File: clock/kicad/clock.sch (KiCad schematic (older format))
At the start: 79 parts, among them SW1 HOUR, SW2 MIN, SW3 TIME, U1 74HC4060, U10 74HC4511, U11 74HC4511, U12 74HC4511, U13 74HC4511, U14 KCSC02-105, U15 KCSC02-105, U16 KCSC02-105, U17 KCSC02-105, U18 KCSC02-105, U19 KCSC02-105, U2 SN74HC74N, U20 74HC14, U21 74HC157, U3 74HC390, U4 74HC08, U5 74HC390, U6 74HC08, U7 74HC390, U8 74HC4511, U9 74HC4511

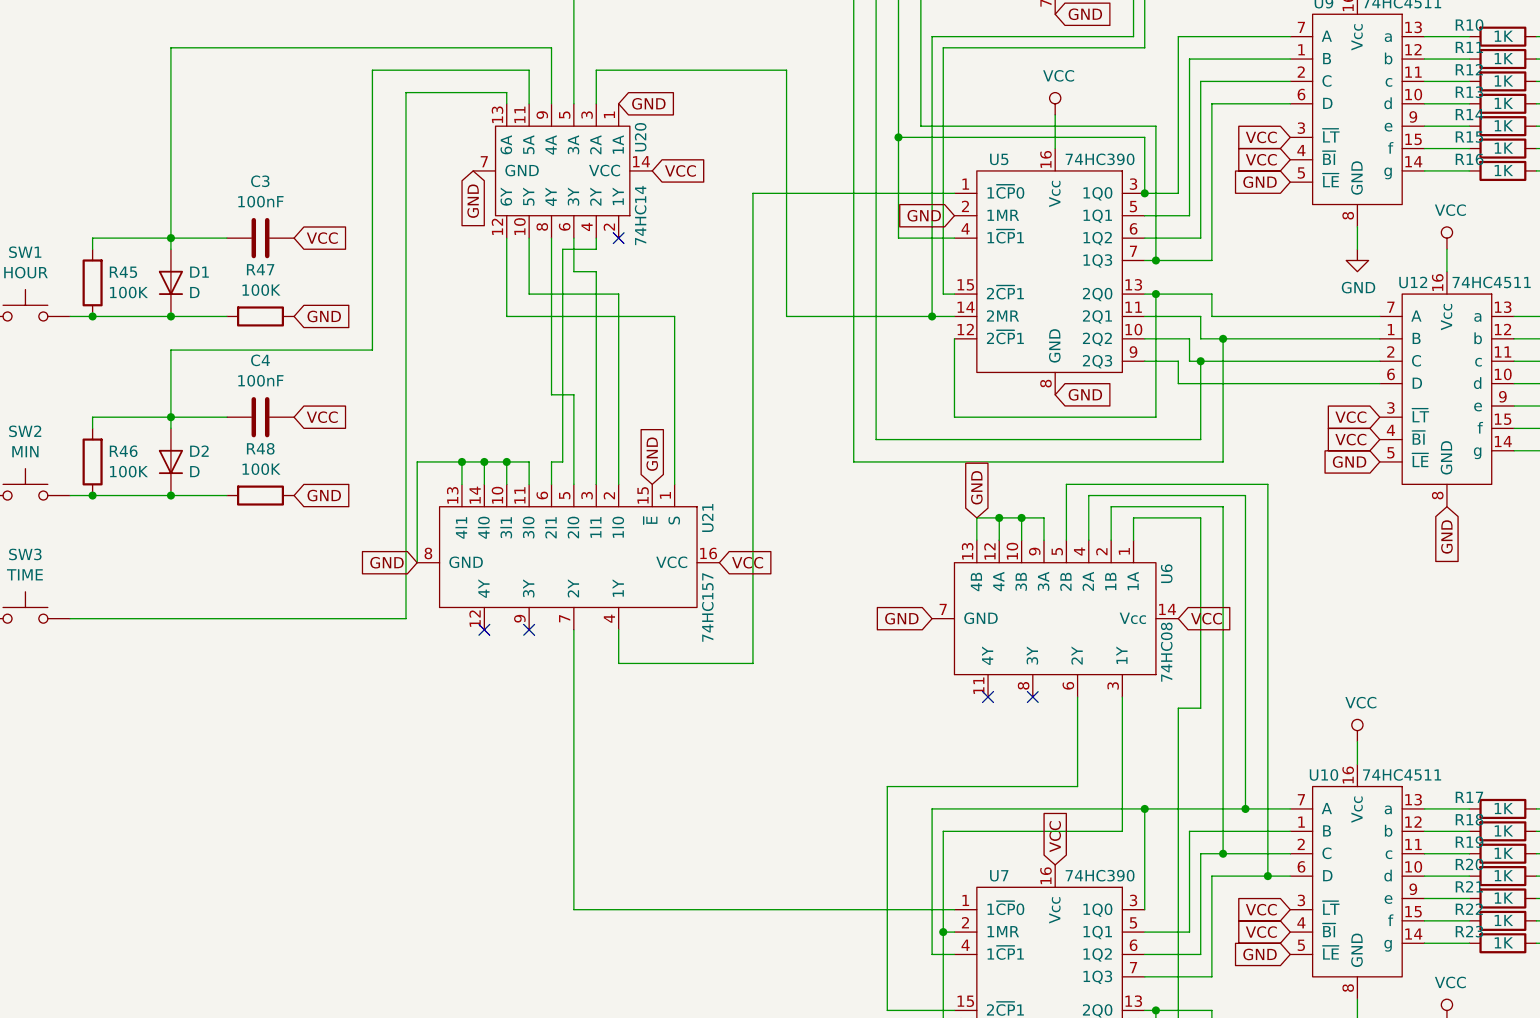
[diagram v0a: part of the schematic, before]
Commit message: Clock: Created PCB Layout.
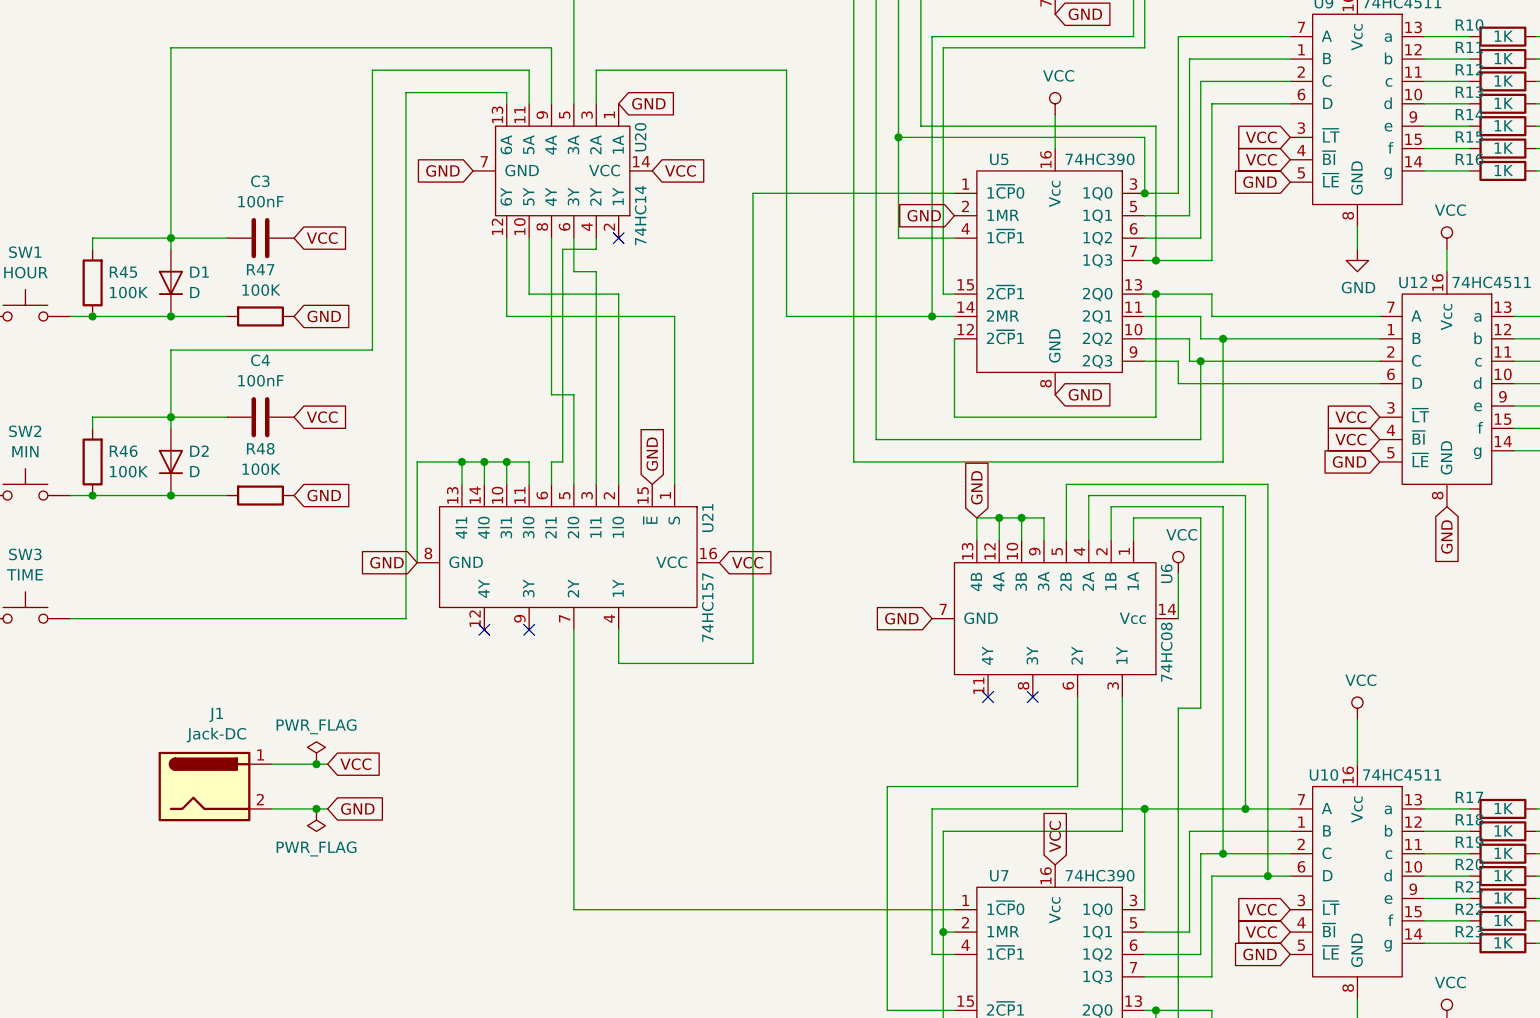
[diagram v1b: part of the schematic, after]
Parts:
- added J1: Jack-DC, KiCad:BarrelJack_CUI_PJ-063AH_Horizontal, symbol Connector:Jack-DC
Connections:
- net GND: now also J1.2
- net VCC: now also J1.1
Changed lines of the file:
@@
 L power:VCC #PWR014
 U 1 1 5D45B0C8
-P 7100 7950
-F 0 "#PWR014" H 7100 7800 50  0001 C CNN
-F 1 "VCC" H 7117 8123 50  0000 C CNN
-F 2 "" H 7100 7950 50  0001 C CNN
-F 3 "" H 7100 7950 50  0001 C CNN
-	1    7100 7950
+P 7100 7850
+F 0 "#PWR014" H 7100 7700 50  0001 C CNN
+F 1 "VCC" H 7117 8023 50  0000 C CNN
+F 2 "" H 7100 7850 50  0001 C CNN
+F 3 "" H 7100 7850 50  0001 C CNN
+	1    7100 7850
 	1    0    0    -1
 $EndComp
@@
 	7100 9100 7100 9200
 Wire Wire Line
-	7100 7950 7100 8050
-Wire Wire Line
 	7500 9200 7500 9300
 Text GLabel 6800 8800 0    50   Input ~ 0
@@
 	5200 8900 5300 8900
 Connection ~ 5200 6050
-Text GLabel 6300 7400 2    50   Input ~ 0
-VCC
 Text GLabel 5200 7400 0    50   Input ~ 0
 GND
@@
 Wire Wire Line
 	1350 7400 2850 7400
-Text GLabel 3150 5400 3    50   Input ~ 0
+Text GLabel 3150 5400 0    50   Input ~ 0
 GND
 Text GLabel 3950 5400 2    50   Input ~ 0
@@
 Connection ~ 3100 6700
 NoConn ~ 3800 5700
+Text GLabel 2900 7150 0    50   Input ~ 0
+GND
+Text GLabel 4250 7150 2    50   Input ~ 0
+VCC
+Wire Wire Line
+	2850 7400 2850 5050
+Wire Wire Line
+	2850 5050 3300 5050
+Wire Wire Line
+	3300 5050 3300 5100
+Wire Wire Line
+	3400 4950 2700 4950
+Wire Wire Line
+	2700 4950 2700 6200
+Wire Wire Line
+	3400 4950 3400 5100
+Wire Wire Line
+	1800 4850 3500 4850
+Wire Wire Line
+	3500 4850 3500 5100
+Wire Wire Line
+	1800 4850 1800 5700
+Wire Wire Line
+	3300 5700 3300 6050
+Wire Wire Line
+	3400 5700 3400 5950
+Wire Wire Line
+	5100 3300 3600 3300
+Wire Wire Line
+	3600 3300 3600 5100
+Connection ~ 5100 3300
+Text GLabel 3800 5100 2    50   Input ~ 0
+GND
+Wire Wire Line
+	5300 5500 4400 5500
+Wire Wire Line
+	4400 5500 4400 7600
+Wire Wire Line
+	4550 6050 4550 4950
+Wire Wire Line
+	4550 4950 3700 4950
+Wire Wire Line
+	3700 4950 3700 5100
+Wire Wire Line
+	4550 6050 5200 6050
+Wire Wire Line
+	4050 6050 4050 6800
+Wire Wire Line
+	3300 6050 4050 6050
+Wire Wire Line
+	3600 7450 3600 8700
+Wire Wire Line
+	3600 8700 5300 8700
+Wire Wire Line
+	3800 7450 3800 7600
+Wire Wire Line
+	3800 7600 4400 7600
+Wire Wire Line
+	3500 5700 3500 6400
+Wire Wire Line
+	3600 6800 3600 6400
+Wire Wire Line
+	3600 6400 3500 6400
+Wire Wire Line
+	3400 5950 3800 5950
+Wire Wire Line
+	3800 5950 3800 6800
+Text GLabel 3950 6800 1    50   Input ~ 0
+GND
+Wire Wire Line
+	3700 5700 3700 5750
+Wire Wire Line
+	3700 5750 3550 5750
+Wire Wire Line
+	3550 6700 3500 6700
+Wire Wire Line
+	3500 6700 3500 6800
+Wire Wire Line
+	2900 7150 2900 6700
+Wire Wire Line
+	2900 6700 3100 6700
+$Comp
+L power:VCC #PWR0101
+U 1 1 5D33EDBB
+P 6300 7200
+F 0 "#PWR0101" H 6300 7050 50  0001 C CNN
+F 1 "VCC" H 6317 7373 50  0000 C CNN
+F 2 "" H 6300 7200 50  0001 C CNN
+F 3 "" H 6300 7200 50  0001 C CNN
+	1    6300 7200
+	1    0    0    -1
+$EndComp
+Wire Wire Line
+	6300 7200 6300 7400
+Wire Wire Line
+	7100 7850 7100 8050
+Wire Wire Line
+	3700 6800 3700 5850
+Wire Wire Line
+	3700 5850 3600 5850
+Wire Wire Line
+	3600 5850 3600 5700
+$Comp
+L Connector:Jack-DC J1
+U 1 1 5D0C7F55
+P 1950 8150
+F 0 "J1" H 2007 8475 50  0000 C CNN
+F 1 "Jack-DC" H 2007 8384 50  0000 C CNN
+F 2 "KiCad:BarrelJack_CUI_PJ-063AH_Horizontal" H 2000 8110 50  0001 C CNN
+F 3 "~" H 2000 8110 50  0001 C CNN
+	1    1950 8150
+	1    0    0    -1
+$EndComp
+Text GLabel 2500 8050 2    50   Input ~ 0
+VCC
+Text GLabel 2500 8250 2    50   Input ~ 0
+GND
+Wire Wire Line
+	2500 8050 2450 8050
+Wire Wire Line
+	2250 8250 2450 8250
+$Comp
+L power:PWR_FLAG #FLG0101
+U 1 1 5D14D41D
+P 2450 8050
+F 0 "#FLG0101" H 2450 8125 50  0001 C CNN
+F 1 "PWR_FLAG" H 2450 8223 50  0000 C CNN
+F 2 "" H 2450 8050 50  0001 C CNN
+F 3 "~" H 2450 8050 50  0001 C CNN
+	1    2450 8050
+	1    0    0    -1
+$EndComp
+Connection ~ 2450 8050
+Wire Wire Line
+	2450 8050 2250 8050
+$Comp
+L power:PWR_FLAG #FLG0102
+U 1 1 5D2210FE
+P 2450 8250
+F 0 "#FLG0102" H 2450 8325 50  0001 C CNN
+F 1 "PWR_FLAG" H 2450 8423 50  0000 C CNN
+F 2 "" H 2450 8250 50  0001 C CNN
+F 3 "~" H 2450 8250 50  0001 C CNN
+	1    2450 8250
+	-1   0    0    1
+$EndComp
+Connection ~ 2450 8250
+Wire Wire Line
+	2450 8250 2500 8250
+Wire Wire Line
+	3550 5750 3550 6700
 $Comp
 L clock:74HC14 U20
@@
 	0    1    1    0
 $EndComp
-Text GLabel 2900 7150 0    50   Input ~ 0
-GND
-Text GLabel 4250 7150 2    50   Input ~ 0
-VCC
-Wire Wire Line
-	2850 7400 2850 5050
-Wire Wire Line
-	2850 5050 3300 5050
-Wire Wire Line
-	3300 5050 3300 5100
-Wire Wire Line
-	3400 4950 2700 4950
-Wire Wire Line
-	2700 4950 2700 6200
-Wire Wire Line
-	3400 4950 3400 5100
-Wire Wire Line
-	1800 4850 3500 4850
-Wire Wire Line
-	3500 4850 3500 5100
-Wire Wire Line
-	1800 4850 1800 5700
-Wire Wire Line
-	3300 5700 3300 6050
-Wire Wire Line
-	3400 5700 3400 5950
-Wire Wire Line
-	5100 3300 3600 3300
-Wire Wire Line
-	3600 3300 3600 5100
-Connection ~ 5100 3300
-Wire Wire Line
-	3600 5700 3600 5850
-Text GLabel 3800 5100 2    50   Input ~ 0
-GND
-Wire Wire Line
-	5300 5500 4400 5500
-Wire Wire Line
-	4400 5500 4400 7600
-Wire Wire Line
-	4550 6050 4550 4950
-Wire Wire Line
-	4550 4950 3700 4950
-Wire Wire Line
-	3700 4950 3700 5100
-Wire Wire Line
-	4550 6050 5200 6050
-Wire Wire Line
-	4050 6050 4050 6800
-Wire Wire Line
-	3300 6050 4050 6050
-Wire Wire Line
-	3600 7450 3600 8700
-Wire Wire Line
-	3600 8700 5300 8700
-Wire Wire Line
-	3800 7450 3800 7600
-Wire Wire Line
-	3800 7600 4400 7600
-Wire Wire Line
-	3500 5700 3500 6400
-Wire Wire Line
-	3600 6800 3600 6400
-Wire Wire Line
-	3600 6400 3500 6400
-Wire Wire Line
-	3600 5850 3700 5850
-Wire Wire Line
-	3700 5850 3700 6800
-Wire Wire Line
-	3400 5950 3800 5950
-Wire Wire Line
-	3800 5950 3800 6800
-Text GLabel 3950 6800 1    50   Input ~ 0
-GND
-Wire Wire Line
-	3700 5700 3700 5750
-Wire Wire Line
-	3700 5750 3550 5750
-Wire Wire Line
-	3550 5750 3550 6700
-Wire Wire Line
-	3550 6700 3500 6700
-Wire Wire Line
-	3500 6700 3500 6800
-Wire Wire Line
-	2900 7150 2900 6700
-Wire Wire Line
-	2900 6700 3100 6700
 $EndSCHEMATC

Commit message: Clock: Added Decoupling Capacitors.
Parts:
- added C10, C11, C12, C13, C14, C15, C16, C17, C18, C19, C5, C6, C8, C9: 100nF, Capacitor_THT:C_Disc_D5.0mm_W2.5mm_P2.50mm, symbol Device:C
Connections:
- net GND: now also C10.2, C11.2, C12.2, C13.2, C14.2, C15.2, C16.2, C17.2, C18.2, C19.2, C5.2, C6.2, C8.2, C9.1
- net VCC: now also C10.1, C11.1, C12.1, C13.1, C14.1, C15.1, C16.1, C17.1, C18.1, C19.1, C5.1, C6.1, C8.1, C9.2

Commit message: Clock: Added USB power connector.
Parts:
- removed J1: Jack-DC, KiCad:BarrelJack_CUI_PJ-063AH_Horizontal, symbol Connector:Jack-DC
- added J1: USB-SS-52100-001, KiCad:USB_A_Stewart_SS-52100-001_Horizontal, symbol clock:USB-SS-52100-001
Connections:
- net GND: now also J1.4 (GND), J1.5 (SHELL)
- net VCC: now also J1.1 (VCC)
- no-connect marks 30 -> 32
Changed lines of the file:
@@
 Wire Wire Line
 	3600 5850 3600 5700
-$Comp
-L Connector:Jack-DC J1
-U 1 1 5D0C7F55
-P 1950 8150
-F 0 "J1" H 2007 8475 50  0000 C CNN
-F 1 "Jack-DC" H 2007 8384 50  0000 C CNN
-F 2 "KiCad:BarrelJack_CUI_PJ-063AH_Horizontal" H 2000 8110 50  0001 C CNN
-F 3 "~" H 2000 8110 50  0001 C CNN
-	1    1950 8150
-	1    0    0    -1
-$EndComp
-Text GLabel 2500 8050 2    50   Input ~ 0
+Text GLabel 2150 8300 2    50   Input ~ 0
 VCC
-Text GLabel 2500 8250 2    50   Input ~ 0
-GND
-Wire Wire Line
-	2500 8050 2450 8050
-Wire Wire Line
-	2250 8250 2450 8250
+Text GLabel 2150 8000 2    50   Input ~ 0
+GND
+Wire Wire Line
+	2150 8300 2100 8300
 $Comp
 L power:PWR_FLAG #FLG0101
 U 1 1 5D14D41D
-P 2450 8050
-F 0 "#FLG0101" H 2450 8125 50  0001 C CNN
-F 1 "PWR_FLAG" H 2450 8223 50  0000 C CNN
-F 2 "" H 2450 8050 50  0001 C CNN
-F 3 "~" H 2450 8050 50  0001 C CNN
-	1    2450 8050
-	1    0    0    -1
-$EndComp
-Connection ~ 2450 8050
-Wire Wire Line
-	2450 8050 2250 8050
+P 2100 8300
+F 0 "#FLG0101" H 2100 8375 50  0001 C CNN
+F 1 "PWR_FLAG" H 2100 8473 50  0000 C CNN
+F 2 "" H 2100 8300 50  0001 C CNN
+F 3 "~" H 2100 8300 50  0001 C CNN
+	1    2100 8300
+	1    0    0    -1
+$EndComp
+Connection ~ 2100 8300
 $Comp
 L power:PWR_FLAG #FLG0102
 U 1 1 5D2210FE
-P 2450 8250
-F 0 "#FLG0102" H 2450 8325 50  0001 C CNN
-F 1 "PWR_FLAG" H 2450 8423 50  0000 C CNN
-F 2 "" H 2450 8250 50  0001 C CNN
-F 3 "~" H 2450 8250 50  0001 C CNN
-	1    2450 8250
-	-1   0    0    1
-$EndComp
-Connection ~ 2450 8250
-Wire Wire Line
-	2450 8250 2500 8250
+P 2100 8000
+F 0 "#FLG0102" H 2100 8075 50  0001 C CNN
+F 1 "PWR_FLAG" H 2100 8173 50  0000 C CNN
+F 2 "" H 2100 8000 50  0001 C CNN
+F 3 "~" H 2100 8000 50  0001 C CNN
+	1    2100 8000
+	1    0    0    -1
+$EndComp
+Connection ~ 2100 8000
+Wire Wire Line
+	2100 8000 2150 8000
 Wire Wire Line
 	3550 5750 3550 6700
@@
 Wire Wire Line
 	3200 1050 4100 1050
+Wire Wire Line
+	1650 8000 2100 8000
+Wire Wire Line
+	1650 8300 2100 8300
+NoConn ~ 1650 8100
+NoConn ~ 1650 8200
+Text GLabel 1450 8500 3    50   Input ~ 0
+GND
+$Comp
+L clock:USB-SS-52100-001 J1
+U 1 1 5D8F04E6
+P 1350 8200
+F 0 "J1" H 1470 8712 60  0000 C CNN
+F 1 "USB-SS-52100-001" H 1470 8606 60  0000 C CNN
+F 2 "KiCad:USB_A_Stewart_SS-52100-001_Horizontal" H 1550 8400 60  0001 L CNN
+F 3 "https://belfuse.com/resources/drawings/stewartconnector/dr-stw-ss-52100-001.pdf" H 1550 8500 60  0001 L CNN
+F 4 "380-1412-ND" H 1550 8600 60  0001 L CNN "Digi-Key_PN"
+F 5 "SS-52100-001" H 1550 8700 60  0001 L CNN "MPN"
+F 6 "Connectors, Interconnects" H 1550 8800 60  0001 L CNN "Category"
+F 7 "USB, DVI, HDMI Connectors" H 1550 8900 60  0001 L CNN "Family"
+F 8 "https://www.digikey.com/product-detail/en/stewart-connector/SS-52100-001/380-1412-ND/7902377" H 1550 9100 60  0001 L CNN "DK_Detail_Page"
+F 9 "CONN RCPT USB2.0 TYPEA 4POS R/A" H 1550 9200 60  0001 L CNN "Description"
+F 10 "Stewart Connector" H 1550 9300 60  0001 L CNN "Manufacturer"
+F 11 "Active" H 1550 9400 60  0001 L CNN "Status"
+	1    1350 8200
+	1    0    0    -1
+$EndComp
 $EndSCHEMATC

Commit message: Clock: Added Photoresistor Driven Pulse Width Modulation for 7-Segment Display Brightness.
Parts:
- added C20: 10nF, Capacitor_THT:C_Disc_D5.0mm_W2.5mm_P2.50mm, symbol Device:C
- added C21, C7: 100nF, Capacitor_THT:C_Disc_D5.0mm_W2.5mm_P2.50mm, symbol Device:C
- added D3, D4: D, digikey-footprints:Diode_DO-35_P10mm, symbol Device:D
- added Q1: PN2222A, Package_TO_SOT_THT:TO-92_Inline, symbol Transistor_BJT:PN2222A
- added R49: VT93xx, OptoDevice:R_LDR_4.9x4.2mm_P2.54mm_Vertical, symbol Sensor_Optical:VT93xx
- added R50, R51: 100K, Resistor_THT:R_Axial_DIN0207_L6.3mm_D2.5mm_P7.62mm_Horizontal, symbol Device:R
- added U22: NE555P, digikey-footprints:DIP-8_W7.62mm, symbol dk_Clock-Timing-Programmable-Timers-and-Oscillators:NE555P
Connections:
- net GND: now also C20.2, C21.2, C7.2, Q1.1 (E), U22.1 (GND); no longer U14.3 (CC), U14.8 (CC), U15.3 (CC), U15.8 (CC), U16.3 (CC), U16.8 (CC), U17.3 (CC), U17.8 (CC), U18.3 (CC), U18.8 (CC), U19.3 (CC), U19.8 (CC)
- net VCC: now also C21.1, U22.4 (RESET), U22.8 (VCC)
- new net: Q1.3 (C), U14.3 (CC), U14.8 (CC), U15.3 (CC), U15.8 (CC), U16.3 (CC), U16.8 (CC), U17.3 (CC), U17.8 (CC), U18.3 (CC), U18.8 (CC), U19.3 (CC), U19.8 (CC)
- new net: C7.1, D3.1 (K), D4.2 (A), U22.2 (TRIG), U22.6 (THRES)
- new net: R51.2, U22.3 (OUT)
- new net: C20.1, U22.5 (CONT)
- new net: D3.2 (A), R49.1, R50.2, U22.7 (DISCH)
- new net: D4.1 (K), R49.2, R50.1
- new net: Q1.2 (B), R51.1

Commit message: Clock: Added decoupling capacitor to 74hc74 flip flop.
Also added fifth mounting hole in the middle of the board.
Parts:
- added C22: 100nF, Capacitor_THT:C_Disc_D5.0mm_W2.5mm_P2.50mm, symbol Device:C
- added R52: 1K, Resistor_THT:R_Axial_DIN0207_L6.3mm_D2.5mm_P7.62mm_Horizontal, symbol Device:R
- Q1: footprint Package_TO_SOT_THT:TO-92_Inline -> Package_TO_SOT_THT:TO-92_Inline_Wide
- U22: footprint digikey-footprints:DIP-8_W7.62mm -> Package_DIP:DIP-8_W7.62mm_Socket
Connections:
- net GND: now also C22.2
- net VCC: now also C22.1, R52.1
- net at D3.2 (A), R49.1, R50.2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: now also R52.2
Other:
- moved on the sheet: C20, C21, C5, C7, D3, D4, Q1, R49, R50, R51, U22

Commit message: Clock: Isolated Crystal Circuit.
Also removed the gap between the 7-segment displays of each cluster.
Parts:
- C1: value 10pF -> 20pF
- C2: value 22pF -> 20pF

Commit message: Clock: Changed footprints for larger ICs.
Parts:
- U20, U4, U6: footprint Package_DIP:DIP-14_W7.62mm_Socket -> clock:Socket_DIP-14_0.775in_Conn
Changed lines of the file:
@@
 	7500 3250 7500 3350
-$Comp
-L clock:74HC08 U4
-U 1 1 5D07855E
-P 5750 4150
-F 0 "U4" H 5550 4650 50  0000 C CNN
-F 1 "74HC08" H 5900 4650 50  0000 C CNN
-F 2 "Package_DIP:DIP-14_W7.62mm_Socket" H 5750 4250 50  0001 C CNN
-F 3 "" H 5750 4250 50  0001 C CNN
-	1    5750 4150
-	1    0    0    -1
-$EndComp
 $Comp
 L power:VCC #PWR08
@@
 	6200 3000 5350 3000
 Wire Wire Line
-	5350 3000 5350 3800
-Wire Wire Line
 	5350 3800 5400 3800
 Wire Wire Line
@@
 Wire Wire Line
 	6450 2600 6450 3150
-Wire Wire Line
-	6450 3150 5250 3150
-Wire Wire Line
-	5250 3150 5250 4100
-Wire Wire Line
-	5250 4100 5400 4100
 Connection ~ 6450 2600
 Wire Wire Line
 	6450 2600 7200 2600
-Wire Wire Line
-	6500 3200 5300 3200
-Wire Wire Line
-	5300 3200 5300 4000
-Wire Wire Line
-	5300 4000 5400 4000
 Wire Wire Line
 	6300 2700 7200 2700
@@
 Wire Wire Line
 	5100 3300 6250 3300
-Wire Wire Line
-	6250 3300 6250 4050
-Wire Wire Line
-	6250 4050 6100 4050
 Text GLabel 6800 1700 0    50   Input ~ 0
 VCC
@@
 	6100 4250 6150 4250
 Wire Wire Line
-	6150 4250 6150 4850
-Wire Wire Line
 	6150 4850 5250 4850
 Wire Wire Line
@@
 F 0 "U6" H 5550 7900 50  0000 C CNN
 F 1 "74HC08" H 5900 7900 50  0000 C CNN
-F 2 "Package_DIP:DIP-14_W7.62mm_Socket" H 5750 7500 50  0001 C CNN
+F 2 "clock:Socket_DIP-14_0.775in_Conn" H 5750 7500 50  0001 C CNN
 F 3 "" H 5750 7500 50  0001 C CNN
 	1    5750 7400
@@
 F 0 "U20" H 3400 5750 50  0000 C CNN
 F 1 "74HC14" H 3750 5750 50  0000 C CNN
-F 2 "Package_DIP:DIP-14_W7.62mm_Socket" H 3550 5400 50  0001 C CNN
+F 2 "clock:Socket_DIP-14_0.775in_Conn" H 3550 5400 50  0001 C CNN
 F 3 "" H 3550 5400 50  0001 C CNN
 	1    3550 5400
@@
 	1    0    0    -1
 $EndComp
+Wire Wire Line
+	6500 3200 5300 3200
+Wire Wire Line
+	5350 3000 5350 3800
+Wire Wire Line
+	6450 3150 5250 3150
+Wire Wire Line
+	6150 4250 6150 4850
+Wire Wire Line
+	6250 4050 6100 4050
+Wire Wire Line
+	6250 3300 6250 4050
+Wire Wire Line
+	5300 4000 5400 4000
+Wire Wire Line
+	5300 3200 5300 4000
+Wire Wire Line
+	5250 4100 5400 4100
+Wire Wire Line
+	5250 3150 5250 4100
+$Comp
+L clock:74HC08 U4
+U 1 1 5D07855E
+P 5750 4150
+F 0 "U4" H 5550 4650 50  0000 C CNN
+F 1 "74HC08" H 5900 4650 50  0000 C CNN
+F 2 "clock:Socket_DIP-14_0.775in_Conn" H 5750 4250 50  0001 C CNN
+F 3 "" H 5750 4250 50  0001 C CNN
+	1    5750 4150
+	1    0    0    -1
+$EndComp
